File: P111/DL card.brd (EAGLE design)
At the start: 125.7 x 62.2 mm, 4 parts

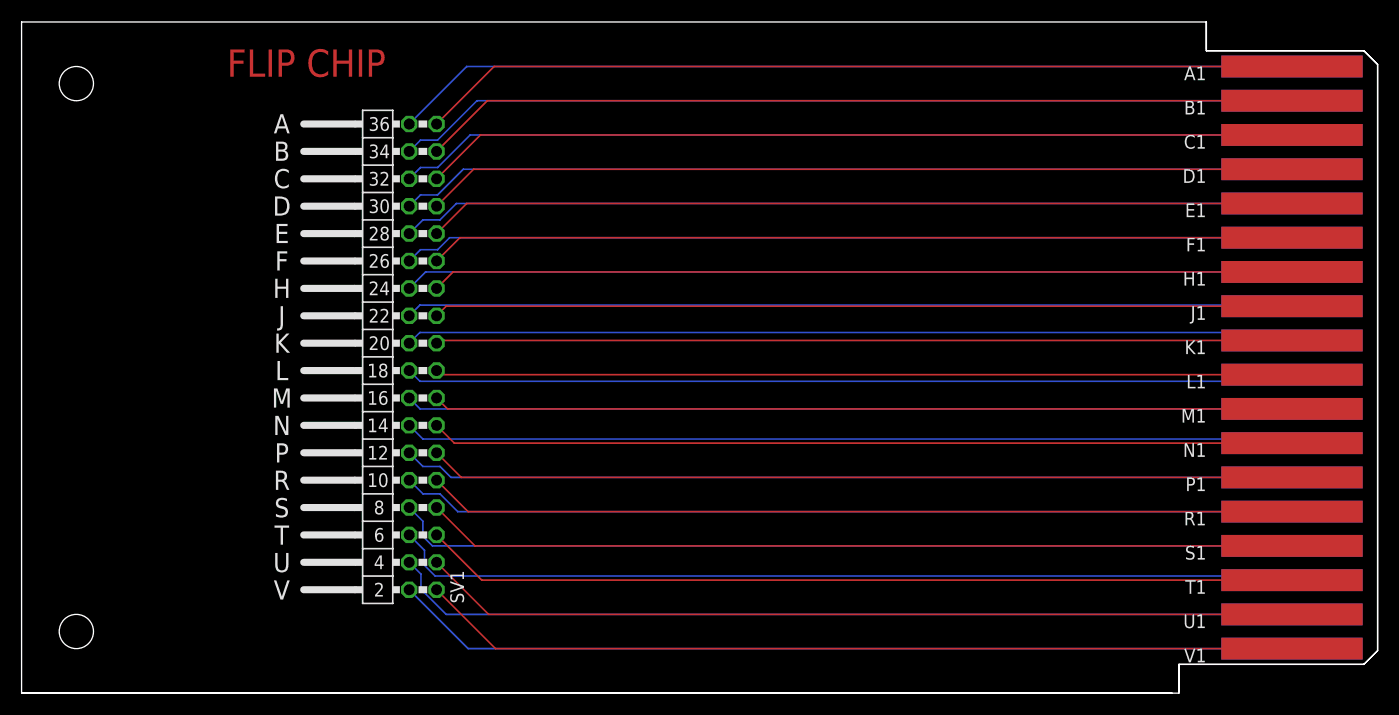
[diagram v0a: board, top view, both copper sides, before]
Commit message: Shrank P111 area to reduce cost
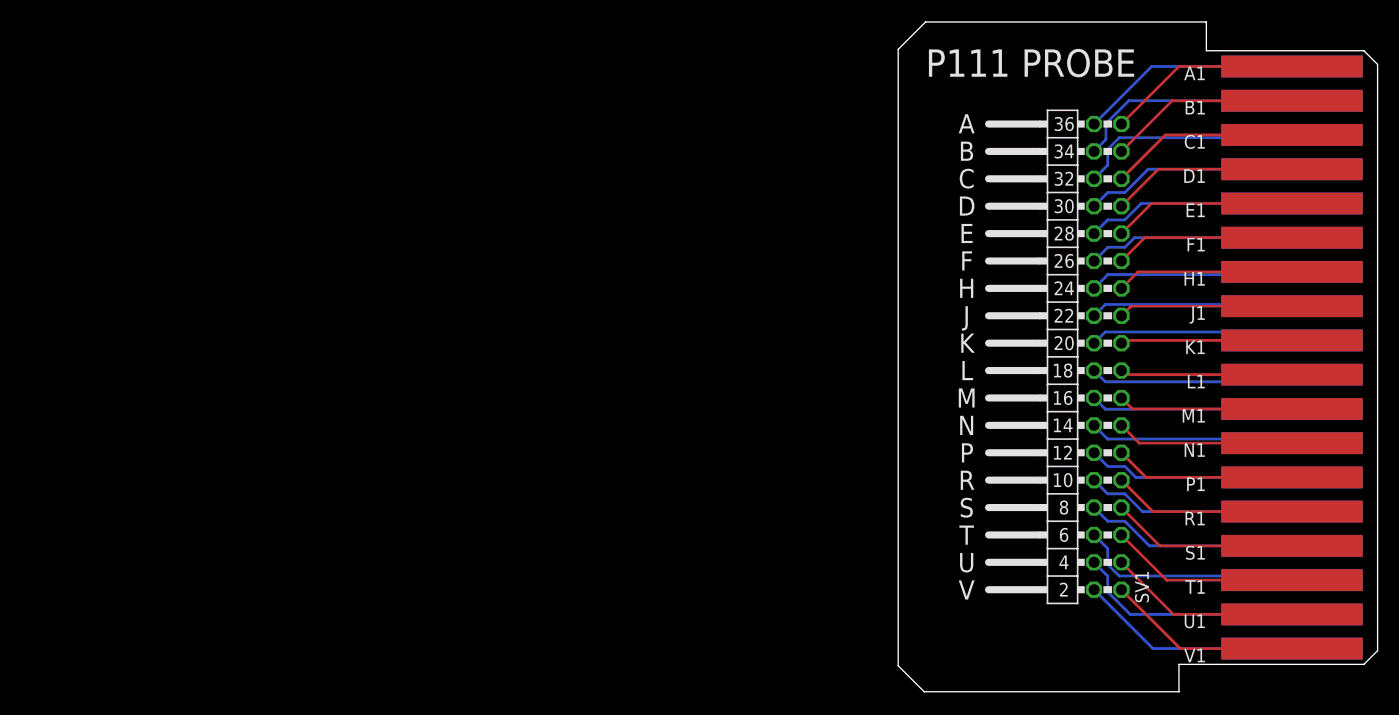
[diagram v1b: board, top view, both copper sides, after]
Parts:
- removed U$1: (no value), dec-con:SINGLE-R
- removed U$2: (no value), dec-con:FLIPCHIP
- moved SV1 63.5 mm to (117.2, 46.4)
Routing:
- net N$4: track 84.1 -> 19.8 mm
- net N$34: track 79.7 -> 16.2 mm
- net N$24: track 80.0 -> 16.5 mm
- net N$12: track 82.5 -> 19.0 mm
- net N$5: track 83.1 -> 19.6 mm
- net N$36: track 79.4 -> 15.9 mm
- net N$35: track 79.5 -> 16.0 mm
- net N$32: track 79.9 -> 16.4 mm
- net N$31: track 80.2 -> 16.7 mm
- net N$30: track 80.5 -> 17.0 mm
- net N$29: track 80.7 -> 17.2 mm
- net N$28: track 81.0 -> 17.5 mm
- net N$27: track 81.3 -> 17.8 mm
- net N$26: track 81.5 -> 18.0 mm
- net N$25: track 80.3 -> 16.8 mm
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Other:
- board size 125.7 x 62.2 mm -> 28.6 x 62.1 mm
- board text added: "P111 PROBE"
